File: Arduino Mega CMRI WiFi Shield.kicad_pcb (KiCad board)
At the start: 2 copper layers, 100 x 56.5 mm, 31 parts, among them IC1 TXS0104ED, IC2 LD1117V33C, J1 M20-7830446, J10 61300411121, J11 61300411121, J12 61300411121, J13 61300411121, J14 61300411121, J15 61300411121, J16 61300411121, J17 61300411121, J18 61300311121, J2 61300411121, J3 61300411121, J4 61300411121, J5 61300411121, J6 61300411121, J7 61300411121, J8 61300411121, J9 61300411121

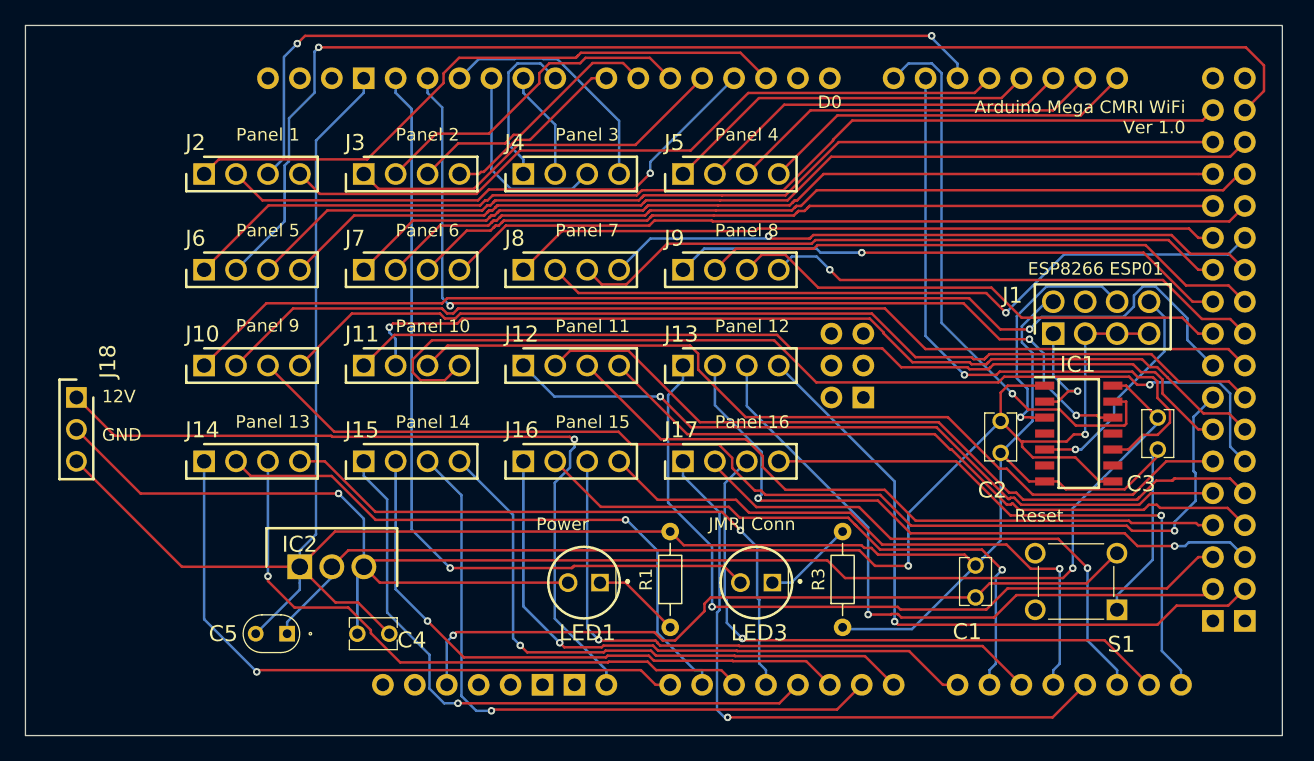
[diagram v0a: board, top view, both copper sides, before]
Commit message: Fixed silkscreen issue when 5V was added to power input header.  Updated board title version to 1.0B.
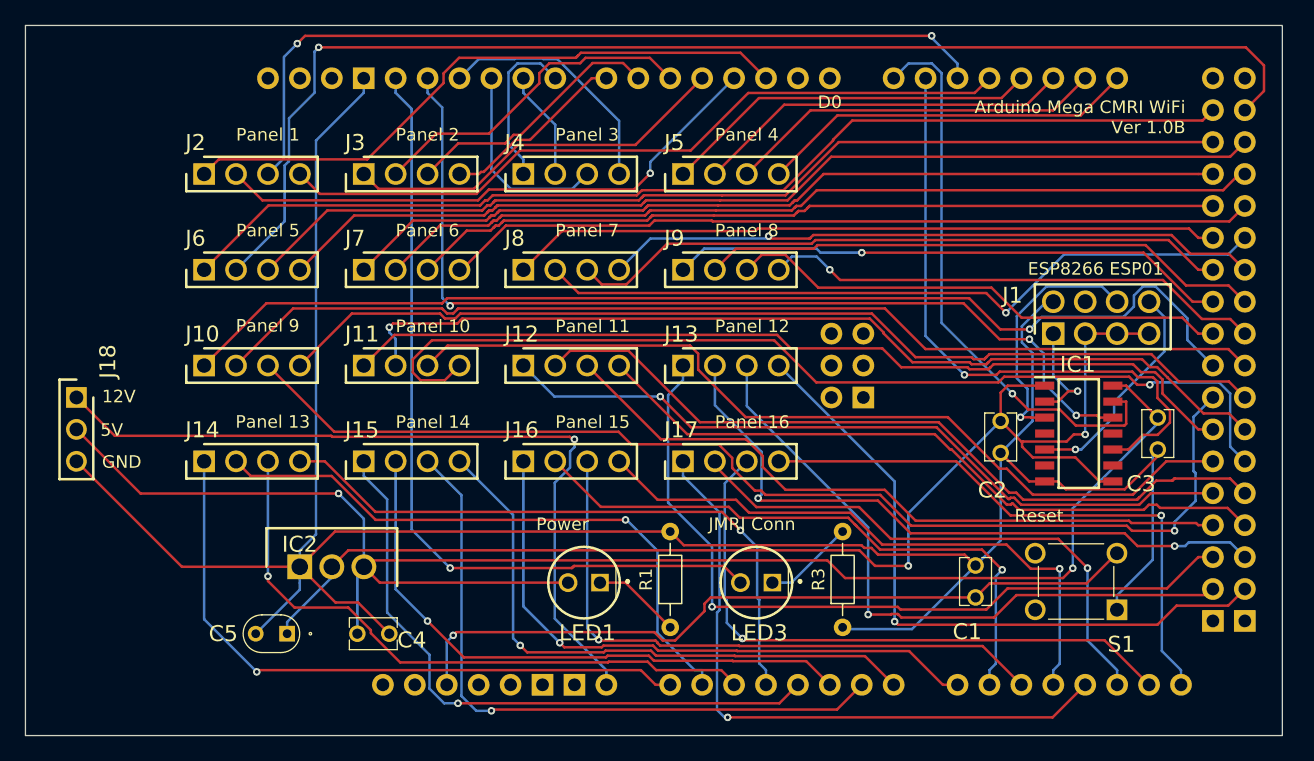
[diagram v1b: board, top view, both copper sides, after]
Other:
- board text added: "5V"
- board text added: "Arduino Mega CMRI WiFi Ver 1.0B"
- board text removed: "Arduino Mega CMRI WiFi Ver 1.0"
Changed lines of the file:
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@@
+		)
+	)
+	(gr_text "5V"
+		(at 88.265 79.375 0)
+		(layer "F.SilkS")
+		(effects
+			(font
+				(size 1 1)
+				(thickness 0.1)
+			)
+			(justify left bottom)
 		)
 	)
@@
 	)
 	(gr_text "GND"
-		(at 88.392 79.756 0)
+		(at 88.392 81.915 0)
 		(layer "F.SilkS")
 		(effects
@@
 		)
 	)
-	(gr_text "Arduino Mega CMRI WiFi\nVer 1.0"
+	(gr_text "Arduino Mega CMRI WiFi\nVer 1.0B"
 		(at 174.6 55.3 0)
 		(layer "F.SilkS")

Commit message: Swapped components for those in custom library, updated labelling on PCB.
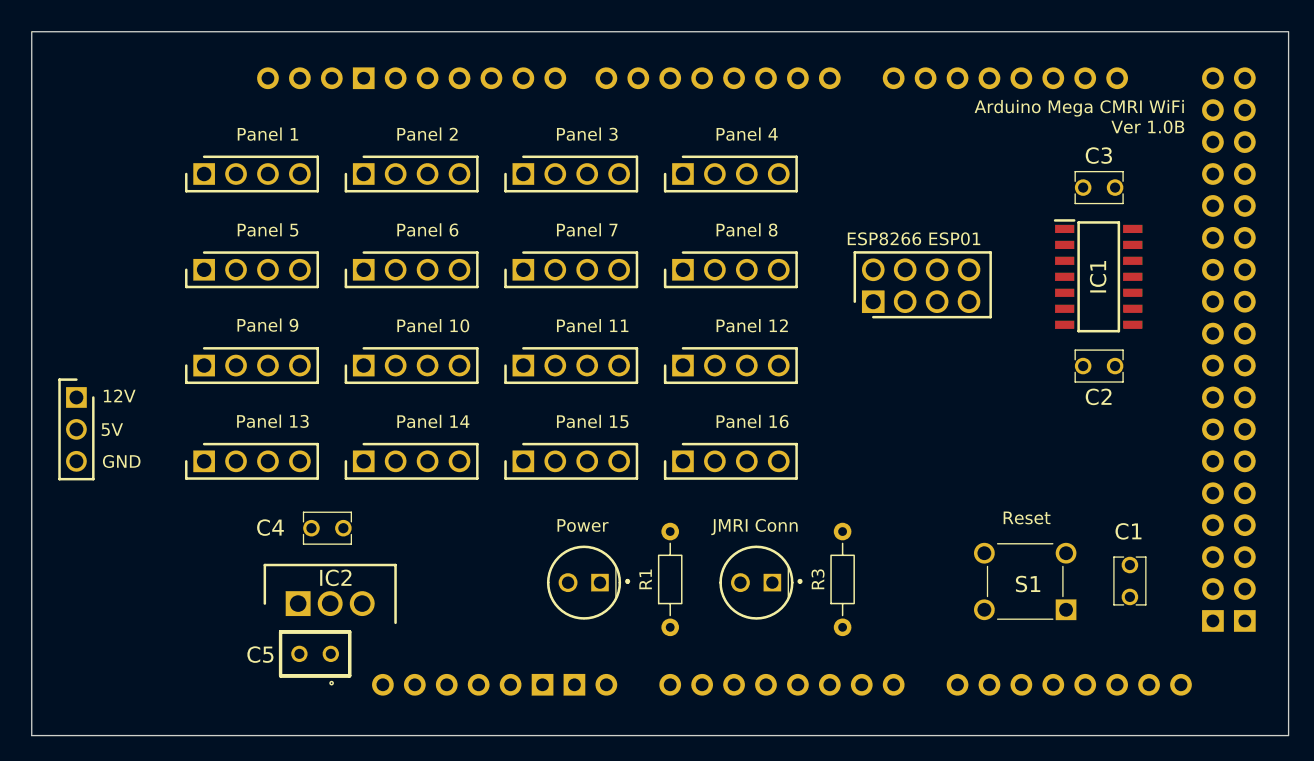
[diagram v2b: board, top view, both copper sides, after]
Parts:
- A1: value Arduino_Mega2560_R3_Shield -> SBC-ArduinoMega2560R3Shield-NoSPI; footprint PCM_arduino-library:Arduino_Mega2560_R3_Shield -> Custom:SBC-ArduinoMega2560R3Shield-NoSPI
- C1, C2, C3, C4: value C315C104M5U5TA -> Cap-100nF-50V-TH; footprint SamacSys_Parts:C315C100J2G5TA -> Custom:80-C315C104M5U
- C5: value FG14X7R1A106KRT06 -> Cap-10uF-25V-TH; footprint SamacSys_Parts:FG14 -> Custom:810-FG16X7R1E106KRT6
- IC1: value TXS0104ED -> IC-VLT-5V3.3V-SM; footprint SamacSys_Parts:SOIC127P600X175-14N -> Custom:595-TXS0104ED
- IC2: value LD1117V33C -> VoltageRegulator-5V-3V3-TH; footprint SamacSys_Parts:TO255P460X1020X2008-3P -> Custom:511-LD1117V33C
- J1: value M20-7830446 -> Socket-2x4-TH; footprint SamacSys_Parts:RHDR8W70P254X254_2X4_1056X500X850P -> Custom:855-M20-7830446
- J10, J11, J12, J13, J14, J15, J16, J17, J2, J3, J4, J5, J6, J7, J8, J9: value 61300411121 -> Header-1x4-TH; footprint SamacSys_Parts:HDRV4W95P0X254_1X4_1016X254X854P -> Custom:710-61300411121
- J18: value 61300311121 -> Header-1x3-TH; footprint SamacSys_Parts:HDRV3W64P0X254_1X3_762X254X869P -> Custom:710-61300311121
- LED1: value WP7113GD -> LED-Green-TH; footprint SamacSys_Parts:L53ND -> Custom:604-WP7113GD
- LED3: value WP7113ID -> LED-Red-TH; footprint SamacSys_Parts:L53ND -> Custom:604-WP7113ID
- R1, R3: value CFR-25JB-52-1K -> RES-1K-TH
- S1: value B3F-1006 -> SW-NO-TH; footprint SamacSys_Parts:B3F1006 -> Custom:653-B3F-1006
- moved C3 20.1 mm to (167.7, 59.5), turned to 0 degrees
- moved J1 14.5 mm to (149.8, 68.6)
- moved IC1 12.6 mm to (167.7, 66.6)
- moved C1 12.3 mm to (170.2, 90.8), turned to 90 degrees
- moved C2 9.65 mm to (167.7, 73.7), turned to 180 degrees
- moved C4 9.16 mm to (106.3, 86.6), turned to 180 degrees
- moved S1 4.05 mm to (165.1, 93.1)
- moved IC2 2.93 mm to (104.0, 92.6)
- moved C5 2.74 mm to (105.3, 96.6)
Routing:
- net GND: track 201.1 -> 0.00 mm
- net +5V: track 128.9 -> 0.00 mm, vias 2 -> 0
- net +3V3: track 103.8 -> 0.00 mm, vias 2 -> 0
- net Net-(A1-PadD23): track 100.4 -> 0.00 mm, vias 1 -> 0
- net Net-(A1-PadD40): track 90.3 -> 0.00 mm, vias 1 -> 0
- net Net-(A1-PadD38): track 89.1 -> 0.00 mm, vias 1 -> 0
- net Net-(A1-PadD22): track 85.6 -> 0.00 mm
- net Net-(A1-PadD39): track 84.4 -> 0.00 mm
- net Net-(A1-PadD41): track 80.5 -> 0.00 mm
- net Net-(A1-PadD25): track 80.1 -> 0.00 mm
- net Net-(A1-PadD24): track 79.9 -> 0.00 mm
- net Net-(A1-PadD45): track 79.3 -> 0.00 mm, vias 1 -> 0
- net /ESP8266ESP01WiFi/Connected: track 76.8 -> 0.00 mm, vias 3 -> 0
- net Net-(A1-PadD43): track 76.1 -> 0.00 mm, vias 1 -> 0
- net Net-(A1-PadD42): track 72.9 -> 0.00 mm
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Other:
- board size 100 x 56.5 mm -> 100 x 56 mm

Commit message: Updated sheets with version and date, relaid all traces on PCB.
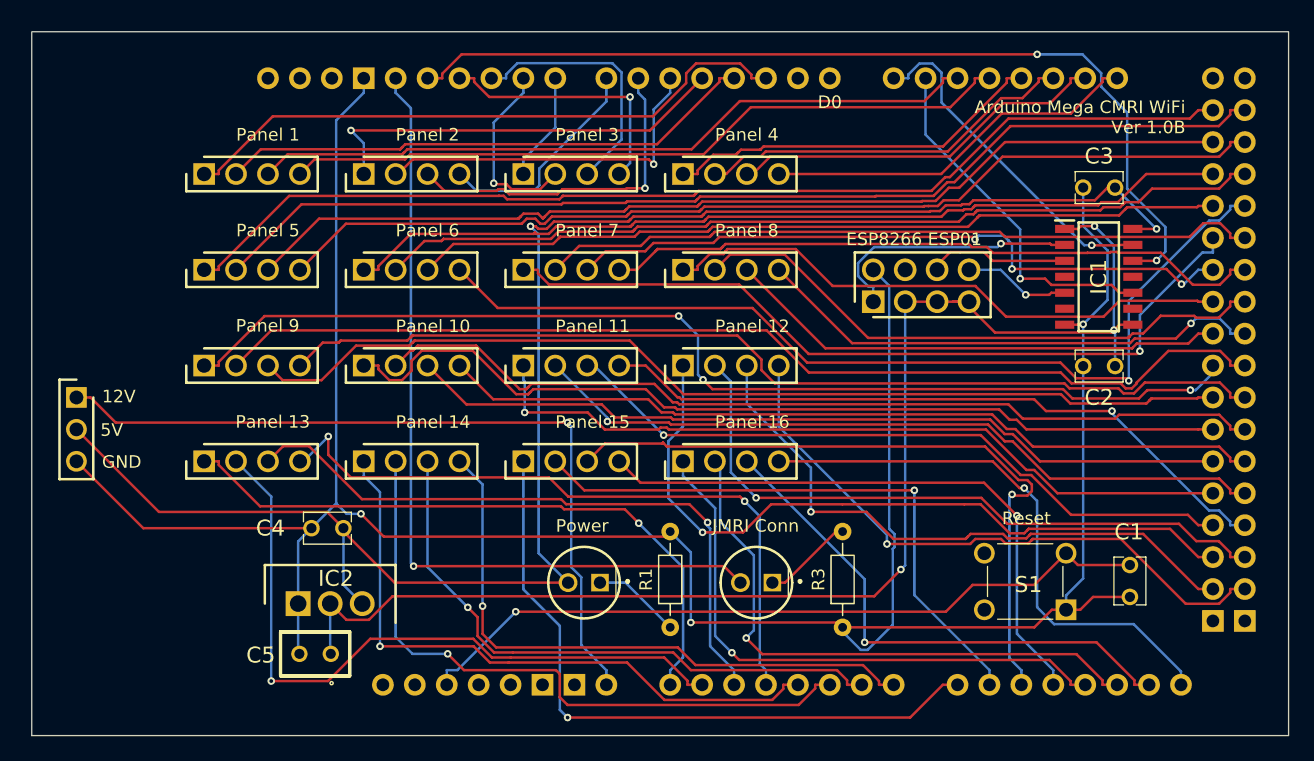
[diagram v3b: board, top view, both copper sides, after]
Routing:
- net GND: track 0.00 -> 212.8 mm, vias 0 -> 3
- net +5V: track 0.00 -> 135.6 mm, vias 0 -> 2
- net +3V3: track 0.00 -> 108.0 mm, vias 0 -> 3
- net Net-(A1-PadD38): track 0.00 -> 88.0 mm, vias 0 -> 3
- net Net-(A1-PadD22): track 0.00 -> 86.1 mm
- net Net-(A1-PadD23): track 0.00 -> 86.0 mm
- net Net-(A1-PadD39): track 0.00 -> 85.3 mm
- net Net-(A1-PadD24): track 0.00 -> 80.6 mm
- net Net-(A1-PadD25): track 0.00 -> 80.3 mm
- net Net-(A1-PadD41): track 0.00 -> 80.1 mm
- net Net-(A1-PadD40): track 0.00 -> 79.7 mm
- net Net-(A1-PadD29): track 0.00 -> 75.8 mm, vias 0 -> 1
- net /ESP8266ESP01WiFi/Connected: track 0.00 -> 74.4 mm, vias 0 -> 2
- net Net-(A1-PadD42): track 0.00 -> 72.8 mm
- net Net-(A1-PadD43): track 0.00 -> 72.2 mm
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
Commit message: Updated PCB for the new logic level module.
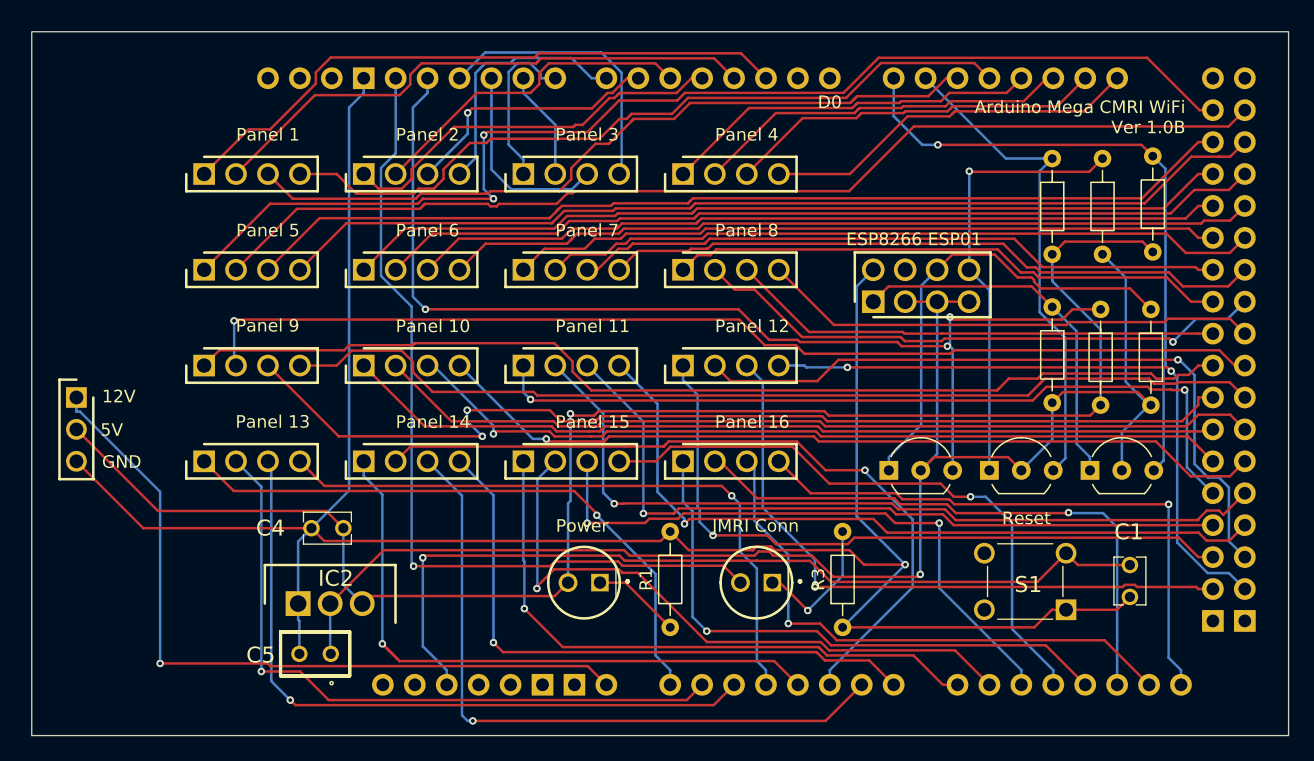
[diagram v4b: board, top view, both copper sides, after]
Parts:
- removed C2, C3: Cap-100nF-50V-TH, Custom:80-C315C104M5U
- removed IC1: IC-VLT-5V3.3V-SM, Custom:595-TXS0104ED
- added Q1: Transistor-FET-.2A-2.6V-TH, Custom:512-2N7000BU, F.Cu at (151.0, 82.0)
- added Q2: Transistor-FET-.2A-2.6V-TH, Custom:512-2N7000BU, F.Cu at (159.0, 82.0)
- added Q3: Transistor-FET-.2A-2.6V-TH, Custom:512-2N7000BU, F.Cu at (167.0, 82.0)
- added R2: Res-10K-TH, Resistor_THT:R_Axial_DIN0204_L3.6mm_D1.6mm_P7.62mm_Horizontal, F.Cu at (171.8, 69.2)
- added R4: Res-10K-TH, Resistor_THT:R_Axial_DIN0204_L3.6mm_D1.6mm_P7.62mm_Horizontal, F.Cu at (167.8, 69.2)
- added R5: Res-10K-TH, Resistor_THT:R_Axial_DIN0204_L3.6mm_D1.6mm_P7.62mm_Horizontal, F.Cu at (168.0, 57.2)
- added R6: Res-10K-TH, Resistor_THT:R_Axial_DIN0204_L3.6mm_D1.6mm_P7.62mm_Horizontal, F.Cu at (164.0, 57.2)
- added R7: Res-10K-TH, Resistor_THT:R_Axial_DIN0204_L3.6mm_D1.6mm_P7.62mm_Horizontal, F.Cu at (164.0, 69.0)
- added R8: Res-10K-TH, Resistor_THT:R_Axial_DIN0204_L3.6mm_D1.6mm_P7.62mm_Horizontal, F.Cu at (172.0, 57.0)
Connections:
- J1 pad 1: Net-(IC1-A1) -> /ESP8266ESP01WiFi/LogicLevelShifter/LOW
- J1 pad 6: Net-(IC1-A2) -> /ESP8266ESP01WiFi/LogicLevelShifter1/LOW
- J1 pad 8: Net-(IC1-A4) -> /ESP8266ESP01WiFi/LogicLevelShifter2/LOW
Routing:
- net GND: track 212.8 -> 174.8 mm, vias 3 -> 1
- net /ESP8266ESP01WiFi/LogicLevelShifter1/LOW: track 0.00 -> 36.9 mm
- net /ESP8266ESP01WiFi/LogicLevelShifter2/LOW: track 0.00 -> 35.5 mm, vias 0 -> 1
- net /ESP8266ESP01WiFi/LogicLevelShifter/LOW: track 0.00 -> 29.7 mm
- net /ESP8266ESP01WiFi/TX: track 27.1 -> 50.8 mm
- net Net-(IC1-A1): track 20.9 -> 0.00 mm, vias 1 -> 0
- net +3V3: track 108.0 -> 125.0 mm, vias 3 -> 1
- net /ESP8266ESP01WiFi/Connected: track 74.4 -> 86.9 mm, vias 2 -> 3
- net Net-(IC1-A2): track 11.2 -> 0.00 mm
- net Net-(A1-PadD29): track 75.8 -> 65.1 mm, vias 1 -> 0
- net /ESP8266ESP01WiFi/RX: track 28.6 -> 39.2 mm, vias 1 -> 0
- net /ArduinoReset/RESET: track 59.8 -> 69.4 mm
- net Net-(IC1-A4): track 8.50 -> 0.00 mm, vias 1 -> 0
- net +5V: track 135.6 -> 127.1 mm, vias 2 -> 1
- net Net-(A1-PadA5): track 52.7 -> 60.5 mm
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
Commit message: Updates look good, promoted to v1.2.
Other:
- board text added: "Arduino Mega CMRI WiFi Ver 1.2"
- board text removed: "Arduino Mega CMRI WiFi Ver 1.0B"
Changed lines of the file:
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@@
 		)
 	)
-	(gr_text "Arduino Mega CMRI WiFi\nVer 1.0B"
+	(gr_text "Arduino Mega CMRI WiFi\nVer 1.2"
 		(at 174.6 55.3 0)
 		(layer "F.SilkS")
